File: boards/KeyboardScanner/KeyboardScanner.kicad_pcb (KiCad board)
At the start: 2 copper layers, 30 parts, among them J1 Keyboard1, J2 Keyboard1, J3 Encoder, U1 74LS151, U10 74LS151, U11 74LS151, U2 74LS151, U3 74LS151, U4 74LS151, U5 ULN2803A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

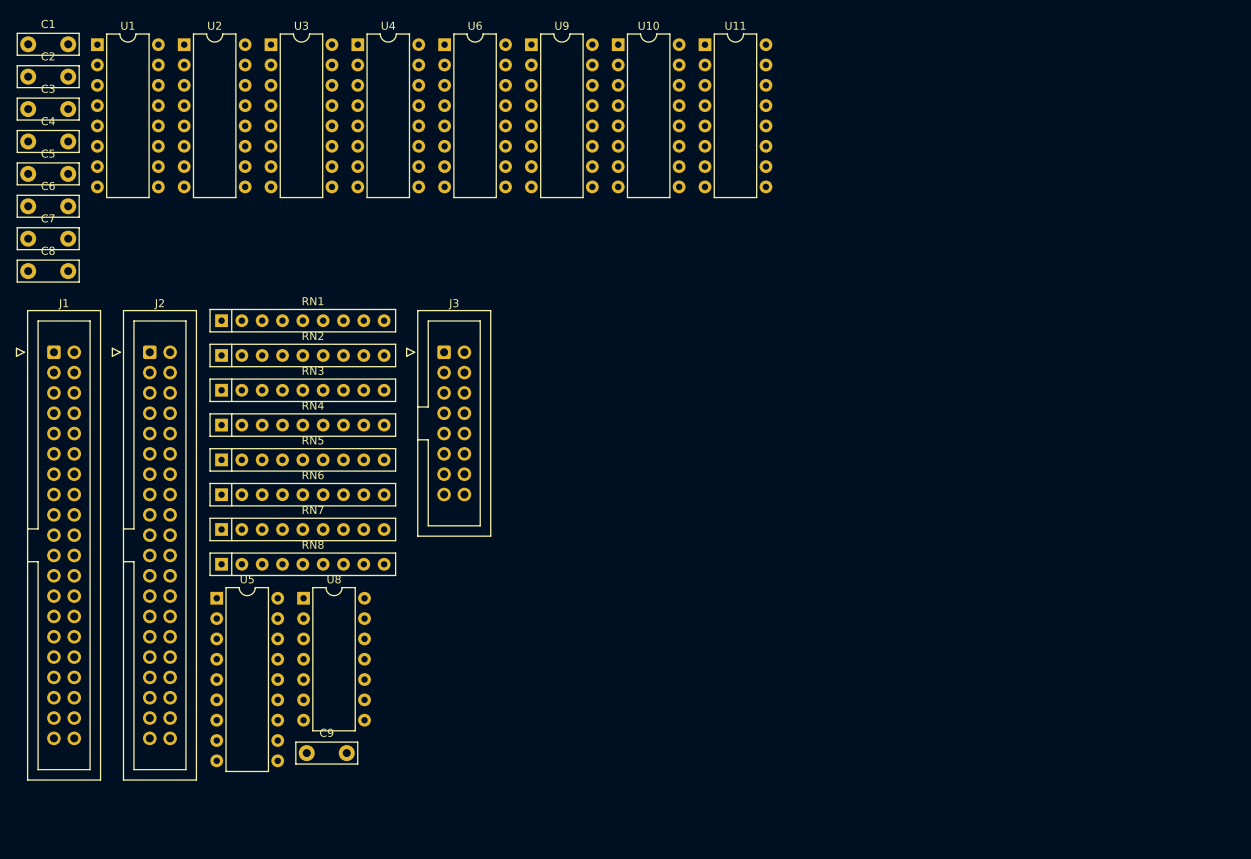
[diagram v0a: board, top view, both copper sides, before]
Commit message: PCB layout for keyboard scanner and piston encoder
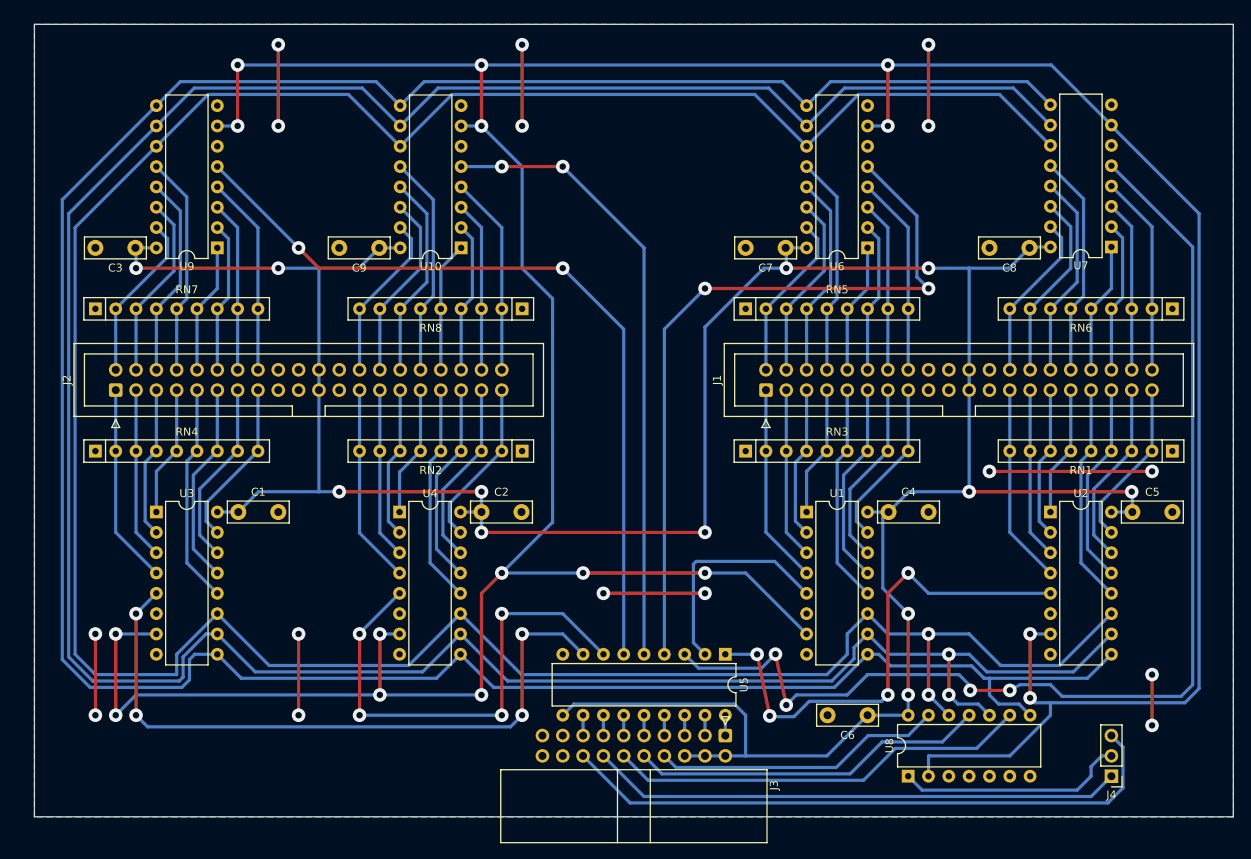
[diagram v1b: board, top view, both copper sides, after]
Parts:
- removed U11: 74LS151, Package_DIP:DIP-16_W7.62mm
- added J4: Select, Connector_PinHeader_2.54mm:PinHeader_1x03_P2.54mm_Vertical, F.Cu at (210.8, 134.6)
- added U7: 74LS151, Package_DIP:DIP-16_W7.62mm, F.Cu at (210.8, 68.5)
- J3: footprint Connector_IDC:IDC-Header_2x08_P2.54mm_Vertical -> Connector_IDC:IDC-Header_2x10_P2.54mm_Horizontal
- moved C5 144.3 mm to (213.4, 101.6)
- moved C8 125.2 mm to (200.6, 68.6), turned to 180 degrees
- moved U2 123.0 mm to (203.2, 101.6)
- moved C6 122.7 mm to (180.3, 127.0), turned to 180 degrees
- moved RN6 121.1 mm to (218.4, 76.2), turned to 180 degrees
- moved RN1 120.0 mm to (218.4, 94.0), turned to 180 degrees
- moved C4 117.1 mm to (183.0, 101.6)
- moved U1 106.2 mm to (172.7, 101.6)
- moved C7 94.7 mm to (170.1, 68.6), turned to 180 degrees
- moved J1 89.1 mm to (167.6, 86.4), turned to 90 degrees
- moved U8 78.8 mm to (185.4, 134.6), turned to 90 degrees
- moved C2 78.6 mm to (132.1, 101.6)
- moved RN5 68.2 mm to (165.1, 76.2)
- moved RN3 65.9 mm to (165.1, 94.0)
- moved C1 64.1 mm to (101.7, 101.6)
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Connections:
- J1 pad 22: unconnected-(J1-Pin_22-Pad22) -> +5V
- J2 pad 22: unconnected-(J2-Pin_22-Pad22) -> +5V
- J3 pad 14: GND -> Net-(J3-Pin_14)
- J3 pad 16: GND -> Net-(J3-Pin_16)
- J3 pad 6: Net-(J3-Pin_6) -> +5V
- RN3 pad 2: K08 -> K01
- RN3 pad 3: K07 -> K02
- RN3 pad 4: K06 -> K03
- RN3 pad 5: K05 -> K04
- RN3 pad 6: K04 -> K05
- RN3 pad 7: K03 -> K06
- RN3 pad 8: K02 -> K07
- RN3 pad 9: K01 -> K08
- RN4 pad 2: K24 -> K17
- RN4 pad 3: K23 -> K18
- RN4 pad 4: K22 -> K19
- RN4 pad 5: K21 -> K20
- RN4 pad 6: K20 -> K21
- RN4 pad 7: K19 -> K22
- RN4 pad 8: K18 -> K23
- RN4 pad 9: K17 -> K24
- U1 pad 12: K08 -> K05
- U1 pad 13: K07 -> K06
- U1 pad 14: K06 -> K07
- U1 pad 15: K05 -> K08
- U10 pad 1: K44 -> K61
- U10 pad 12: K48 -> K60
- U10 pad 13: K47 -> K59
- U10 pad 14: K46 -> K58
- U10 pad 15: K45 -> K57
- U10 pad 2: K43 -> K62
- U10 pad 3: K42 -> K63
- U10 pad 4: K41 -> K64
- U10 pad 5: O6 -> O8
- U2 pad 1: K36 -> K12
- U2 pad 12: K40 -> K13
- U2 pad 13: K39 -> K14
- U2 pad 14: K38 -> K15
- U2 pad 15: K37 -> K16
- U2 pad 2: K35 -> K11
- U2 pad 3: K34 -> K10
- U2 pad 4: K33 -> K09
- U2 pad 5: O5 -> O2
- U3 pad 1: K52 -> K20
- U3 pad 12: K56 -> K21
- U3 pad 13: K55 -> K22
- U3 pad 14: K54 -> K23
- U3 pad 15: K53 -> K24
- U3 pad 2: K51 -> K19
- U3 pad 3: K50 -> K18
- U3 pad 4: K49 -> K17
- U3 pad 5: O7 -> O3
- U4 pad 1: K12 -> K28
- U4 pad 12: K16 -> K29
- U4 pad 13: K15 -> K30
- U4 pad 14: K14 -> K31
- U4 pad 15: K13 -> K32
- U4 pad 2: K11 -> K27
- U4 pad 3: K10 -> K26
- U4 pad 4: K09 -> K25
- U4 pad 5: O2 -> O4
- U5 pad 1: O1 -> O2
- U5 pad 2: O2 -> O1
- U5 pad 3: O3 -> O6
- U5 pad 4: O4 -> O5
- U5 pad 5: O5 -> O8
- U5 pad 6: O6 -> O7
- U5 pad 7: O7 -> O4
- U5 pad 8: O8 -> O3
- U6 pad 1: K20 -> K37
- U6 pad 12: K24 -> K36
- U6 pad 13: K23 -> K35
- U6 pad 14: K22 -> K34
- U6 pad 15: K21 -> K33
- U6 pad 2: K19 -> K38
- U6 pad 3: K18 -> K39
- U6 pad 4: K17 -> K40
- U6 pad 5: O3 -> O5
- U8 pad 1: Net-(J3-Pin_6) -> Net-(J4-Pin_2)
- U8 pad 10: unconnected-(U8-Pad10) -> S1
- U8 pad 11: GND -> Net-(J3-Pin_10)
- U8 pad 12: unconnected-(U8-Pad12) -> S0
- U8 pad 13: GND -> Net-(J3-Pin_8)
- U8 pad 3: Net-(J3-Pin_8) -> GND
- U8 pad 4: S0 -> unconnected-(U8-Pad4)
- U8 pad 5: Net-(J3-Pin_10) -> GND
- U8 pad 6: S1 -> unconnected-(U8-Pad6)
- U9 pad 1: K28 -> K53
- U9 pad 12: K32 -> K52
- U9 pad 13: K31 -> K51
- U9 pad 14: K30 -> K50
- U9 pad 15: K29 -> K49
- U9 pad 2: K27 -> K54
- U9 pad 3: K26 -> K55
- U9 pad 4: K25 -> K56
- U9 pad 5: O4 -> O7
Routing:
- net En: track 0.00 -> 464.0 mm, vias 0 -> 16
- net +5V: track 0.00 -> 368.2 mm, vias 0 -> 12
- net S0: track 0.00 -> 360.5 mm, vias 0 -> 2
- net S1: track 0.00 -> 354.7 mm, vias 0 -> 2
- net S2: track 0.00 -> 345.7 mm
- net O6: track 0.00 -> 143.3 mm, vias 0 -> 4
- net O7: track 0.00 -> 99.9 mm, vias 0 -> 2
- net O5: track 0.00 -> 93.7 mm, vias 0 -> 2
- net GND: track 0.00 -> 90.2 mm, vias 0 -> 16
- net O3: track 0.00 -> 84.6 mm, vias 0 -> 4
- net O8: track 0.00 -> 77.9 mm, vias 0 -> 2
- net Net-(J3-Pin_16): track 0.00 -> 77.8 mm
- net Net-(J3-Pin_14): track 0.00 -> 66.7 mm
- net O2: track 0.00 -> 62.9 mm, vias 0 -> 4
- net O4: track 0.00 -> 62.6 mm, vias 0 -> 4
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- added copper zone on B.Cu, net GND
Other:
- board outline added: 149.9 x 99.1 mm

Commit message: Updated to KiCAD 8, fixed optocouplers for MIDI and added powersupplies
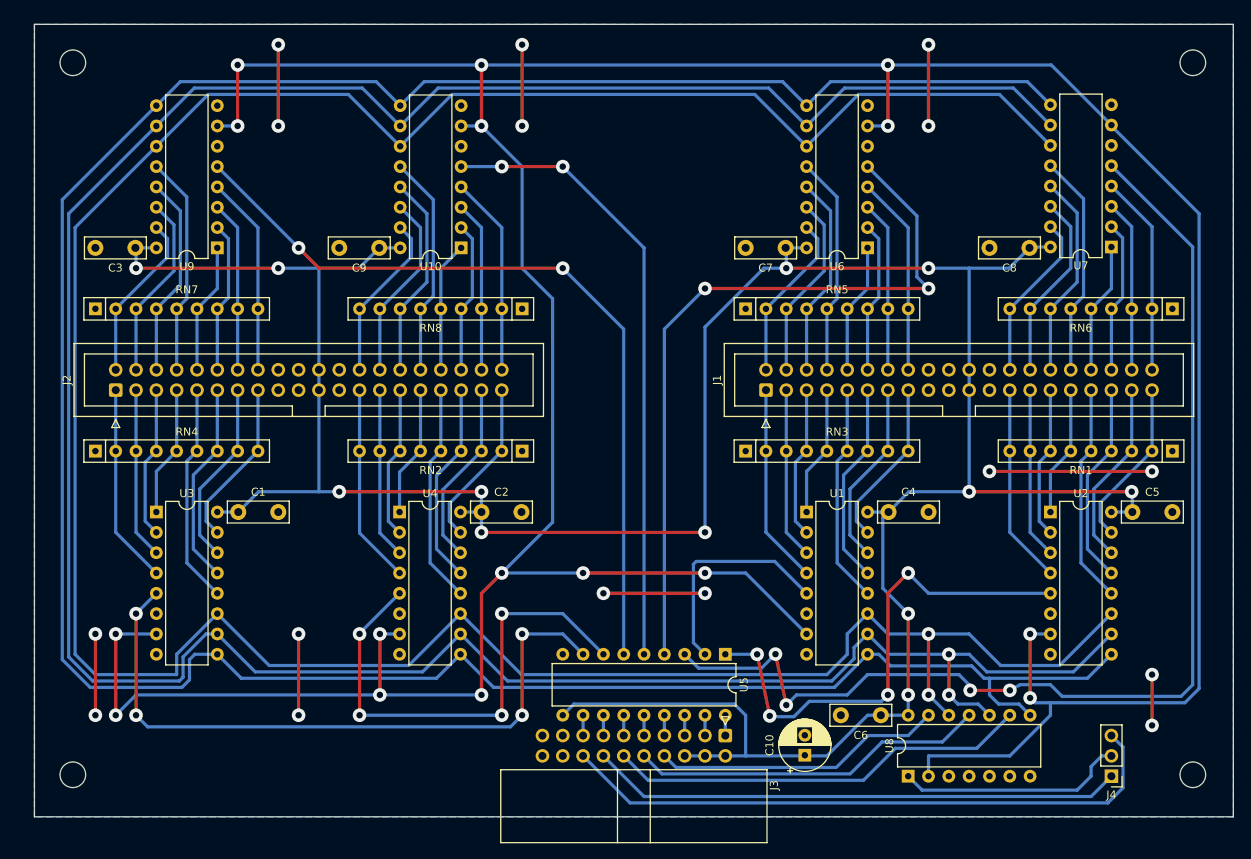
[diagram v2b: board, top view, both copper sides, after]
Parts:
- added C10: 10uF, Capacitor_THT:CP_Radial_D6.3mm_P2.50mm, F.Cu at (172.5, 132.0)
- added H1: MountingHole, MountingHole:MountingHole_3.2mm_M3, F.Cu at (81.0, 134.4)
- added H2: MountingHole, MountingHole:MountingHole_3.2mm_M3, F.Cu at (221.0, 45.4)
- added H3: MountingHole, MountingHole:MountingHole_3.2mm_M3, F.Cu at (81.0, 45.4)
- added H4: MountingHole, MountingHole:MountingHole_3.2mm_M3, F.Cu at (221.0, 134.4)
- moved C6 1.66 mm to (182.0, 127.0)

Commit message: Cleanup of PCB sizes and mounthole positions. Moved MIDI connectors to separate board.
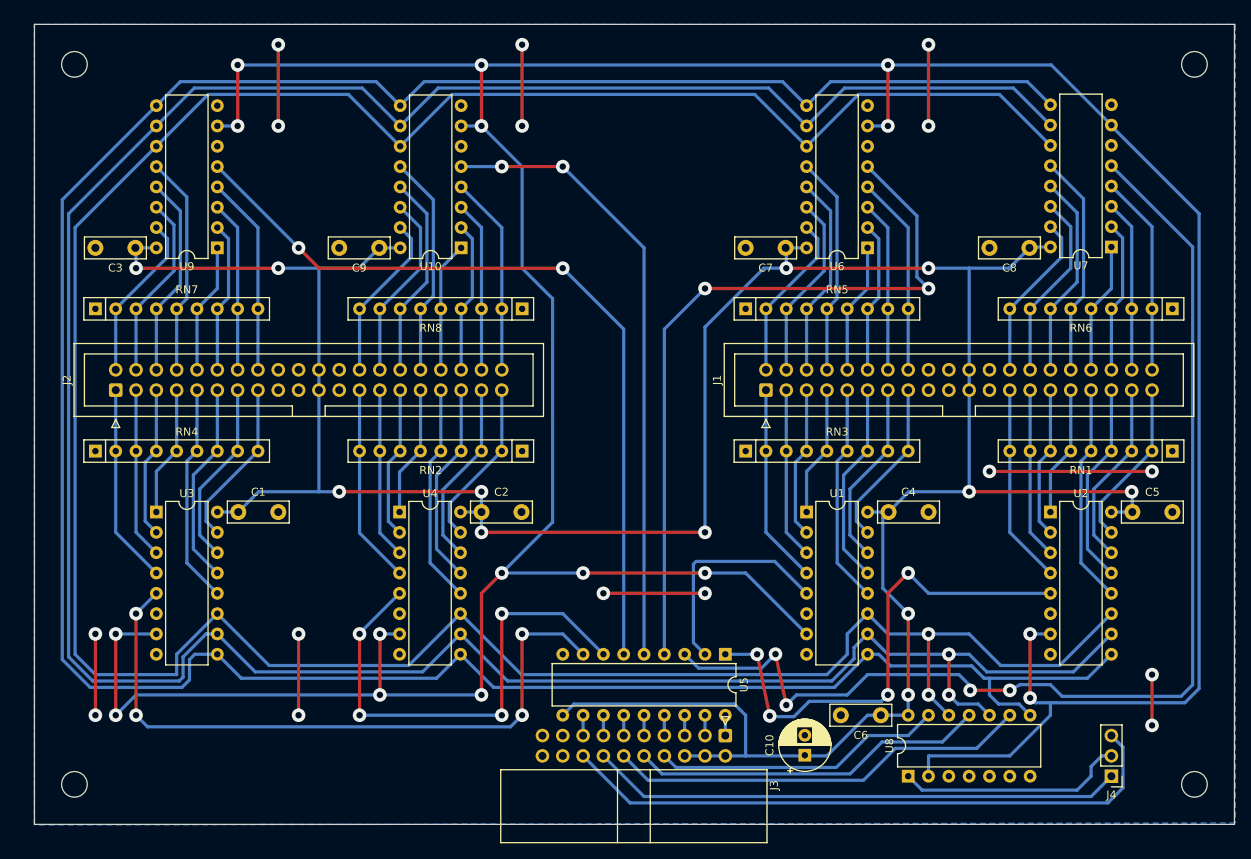
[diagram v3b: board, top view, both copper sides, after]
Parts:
- moved H1 1.22 mm to (81.2, 135.6)
- moved H4 1.22 mm to (221.2, 135.6)
- moved H3 0.28 mm to (81.2, 45.6)
- moved H2 0.28 mm to (221.2, 45.6)
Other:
- board size 149.9 x 99.1 mm -> 150 x 100 mm
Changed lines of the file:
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@@
 		(pad_to_mask_clearance 0)
 		(allow_soldermask_bridges_in_footprints no)
-		(aux_axis_origin 76.2 139.7)
+		(aux_axis_origin 76.2 40.64)
 		(pcbplotparams
 			(layerselection 0x00010fc_ffffffff)
@@
 	(footprint "MountingHole:MountingHole_3.2mm_M3"
 		(layer "F.Cu")
-		(at 81 134.44)
+		(at 81.2 135.64)
 		(descr "Mounting Hole 3.2mm, no annular, M3")
 		(tags "mounting hole 3.2mm no annular m3")
@@
 	(footprint "MountingHole:MountingHole_3.2mm_M3"
 		(layer "F.Cu")
-		(at 81 45.44)
+		(at 81.2 45.64)
 		(descr "Mounting Hole 3.2mm, no annular, M3")
 		(tags "mounting hole 3.2mm no annular m3")
@@
 	(footprint "MountingHole:MountingHole_3.2mm_M3"
 		(layer "F.Cu")
-		(at 221 134.44)
+		(at 221.2 135.64)
 		(descr "Mounting Hole 3.2mm, no annular, M3")
 		(tags "mounting hole 3.2mm no annular m3")
@@
 	(footprint "MountingHole:MountingHole_3.2mm_M3"
 		(layer "F.Cu")
-		(at 221 45.44)
+		(at 221.2 45.64)
 		(descr "Mounting Hole 3.2mm, no annular, M3")
 		(tags "mounting hole 3.2mm no annular m3")
@@
 	(gr_rect
 		(start 76.2 40.64)
-		(end 226.06 139.7)
+		(end 226.2 140.64)
 		(stroke
 			(width 0.05)
@@
 	)
 	(dimension
-		(type aligned)
-		(layer "Cmts.User")
-		(pts
-			(xy 76.2 40.64) (xy 226.06 40.64)
-		)
-		(height -10.16)
-		(gr_text "149,8600 mm"
-			(at 151.13 29.33 0)
-			(layer "Cmts.User")
-			(effects
-				(font
-					(size 1 1)
-					(thickness 0.15)
-				)
-			)
-		)
-		(format
-			(prefix "")
-			(suffix "")
-			(units 3)
-			(units_format 1)
-			(precision 4)
-		)
-		(style
-			(thickness 0.1)
-			(arrow_length 1.27)
-			(text_position_mode 0)
-			(extension_height 0.58642)
-			(extension_offset 0.5) keep_text_aligned)
-	)
-	(dimension
-		(type aligned)
-		(layer "Cmts.User")
-		(pts
-			(xy 226.06 40.64) (xy 226.06 139.7)
-		)
-		(height -10.16)
-		(gr_text "99,0600 mm"
-			(at 235.07 90.17 90)
-			(layer "Cmts.User")
-			(effects
-				(font
-					(size 1 1)
-					(thickness 0.15)
-				)
-			)
-		)
-		(format
-			(prefix "")
-			(suffix "")
-			(units 3)
-			(units_format 1)
-			(precision 4)
-		)
-		(style
-			(thickness 0.1)
-			(arrow_length 1.27)
-			(text_position_mode 0)
-			(extension_height 0.58642)
-			(extension_offset 0.5) keep_text_aligned)
-	)
-	(dimension
 		(type orthogonal)
 		(layer "Cmts.User")
 		(pts
-			(xy 76.2 139.7) (xy 81 134.44)
+			(xy 226.314 40.64) (xy 226.2 140.64)
 		)
-		(height -3.048)
+		(height 7.366)
 		(orientation 1)
-		(gr_text "5,2600 mm"
-			(at 72.002 137.07 90)
+		(gr_text "100,0000 mm"
+			(at 232.53 90.64 90)
 			(layer "Cmts.User")
 			(effects
@@
 		(layer "Cmts.User")
 		(pts
-			(xy 221 134.44) (xy 226.06 139.7)
+			(xy 81.2 45.64) (xy 76.2 40.64)
 		)
-		(height 13.642)
+		(height -9.572)
 		(orientation 0)
-		(gr_text "5,0600 mm"
-			(at 223.53 146.932 0)
+		(gr_text "5,0000 mm"
+			(at 78.7 34.918 0)
 			(layer "Cmts.User")
 			(effects
@@
 		(layer "Cmts.User")
 		(pts
-			(xy 81 135) (xy 221 134)
-		)
-		(height 13)
-		(orientation 0)
-		(gr_text "140,0000 mm"
-			(at 151 146.85 0)
-			(layer "Cmts.User")
-			(effects
-				(font
-					(size 1 1)
-					(thickness 0.15)
-				)
-			)
+			(xy 81.2 135.64) (xy 81.2 45.64)
 		)
-		(format
-			(prefix "")
-			(suffix "")
-			(units 3)
-			(units_format 1)
-			(precision 4)
-		)
-		(style
-			(thickness 0.12)
-			(arrow_length 1.27)
-			(text_position_mode 0)
-			(extension_height 0.58642)
-			(extension_offset 0.5) keep_text_aligned)
-	)
-	(dimension
-		(type orthogonal)
-		(layer "Cmts.User")
-		(pts
-			(xy 81 45) (xy 76.2 40.64)
-		)
-		(height -8)
-		(orientation 0)
-		(gr_text "4,8000 mm"
-			(at 78.6 35.85 0)
+		(height -11.604)
+		(orientation 1)
+		(gr_text "90,0000 mm"
+			(at 68.446 90.64 90)
 			(layer "Cmts.User")
 			(effects
@@
 		(layer "Cmts.User")
 		(pts
-			(xy 76.2 40.64) (xy 81 45.44)
+			(xy 81.2 45.64) (xy 76.2 40.64)
 		)
-		(height -4.064)
+		(height -11.604)
 		(orientation 1)
-		(gr_text "4,8000 mm"
-			(at 70.986 43.04 90)
+		(gr_text "5,0000 mm"
+			(at 68.446 43.14 90)
 			(layer "Cmts.User")
 			(effects
@@
 		(layer "Cmts.User")
 		(pts
-			(xy 81 134.44) (xy 81 45.44)
+			(xy 81.2 135.64) (xy 221.2 135.64)
 		)
-		(height -8.864)
-		(orientation 1)
-		(gr_text "89,0000 mm"
-			(at 70.986 89.94 90)
+		(height 13.458)
+		(orientation 0)
+		(gr_text "140,0000 mm"
+			(at 151.2 147.948 0)
 			(layer "Cmts.User")
 			(effects
@@
 		(layer "Cmts.User")
 		(pts
-			(xy 76.2 139.7) (xy 81 135)
+			(xy 226.2 40.64) (xy 76.2 40.64)
 		)
-		(height 6.3)
+		(height -11.684)
 		(orientation 0)
-		(gr_text "4,8000 mm"
-			(at 78.6 144.85 0)
+		(gr_text "150,0000 mm"
+			(at 151.2 27.806 0)
 			(layer "Cmts.User")
 			(effects
@@
 		)
 		(style
-			(thickness 0.12)
+			(thickness 0.1)
 			(arrow_length 1.27)
 			(text_position_mode 0)
@@
 		(polygon
 			(pts
-				(xy 226.06 139.7) (xy 76.2 139.7) (xy 76.2 40.64) (xy 226.06 40.64)
+				(xy 226.314 140.462) (xy 76.2 140.716) (xy 76.2 40.64) (xy 226.314 40.64)
 			)
 		)

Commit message: Updated design rules to 0.32mm template and exported Gerber files
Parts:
- C10: value 10uF -> 47uF
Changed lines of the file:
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@@
 		(pad_to_mask_clearance 0)
 		(allow_soldermask_bridges_in_footprints no)
-		(aux_axis_origin 76.2 40.64)
+		(aux_axis_origin 76.2 140.716)
 		(pcbplotparams
-			(layerselection 0x00010fc_ffffffff)
+			(layerselection 0x0001060_fffffffe)
 			(plot_on_all_layers_selection 0x0000000_00000000)
 			(disableapertmacros no)
@@
 			(viasonmask no)
 			(mode 1)
-			(useauxorigin no)
+			(useauxorigin yes)
 			(hpglpennumber 1)
 			(hpglpenspeed 20)
@@
 			(outputformat 1)
 			(mirror no)
-			(drillshape 1)
+			(drillshape 0)
 			(scaleselection 1)
-			(outputdirectory "")
+			(outputdirectory "gerber/")
 		)
 	)
@@
 			)
 		)
-		(property "Value" "10uF"
+		(property "Value" "47uF"
 			(at 1.25 4.4 -90)
 			(layer "F.Fab")
@@
 		(hatch edge 0.5)
 		(connect_pads
-			(clearance 0.508)
+			(clearance 0.4)
 		)
-		(min_thickness 0.42)
+		(min_thickness 0.4)
 		(filled_areas_thickness no)
 		(fill yes
@@
 			(thermal_bridge_width 0.5)
 			(island_removal_mode 2)
-			(island_area_min 2)
+			(island_area_min 1)
 		)
 		(polygon

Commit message: Fixed pulldown resistors for KeyboardScanner
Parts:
- RN1, RN2, RN3, RN4, RN5, RN6, RN7, RN8: value 10k -> 470
